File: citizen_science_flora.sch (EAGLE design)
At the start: 90 parts, among them IC1 W25Q64JVXGIQ, J1 SM03B-SRSS-TB(LF)(SN), J2 TYPE-C-31-M-12, J4 60312202114511, J5 60312202114511, U1 RP2350A, U2 APS6404L-3SQR-ZR, U3 ESP32-C3-MINI-1-N4, U4 MIC5504-3.3YM5-T5, U5 BME690, U6 ADM3260ARSZ, U7 ENS210-LQFM, U8 SFH6325-X017TEL0631, U9 AS3935-BQFT, Y1 12MHz

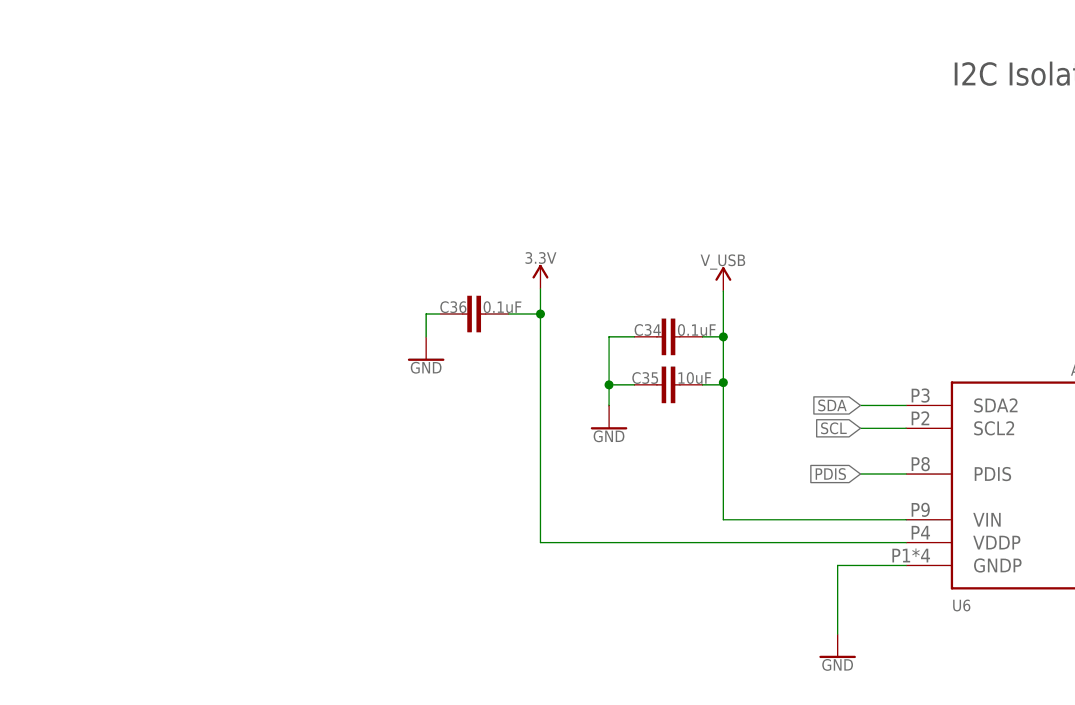
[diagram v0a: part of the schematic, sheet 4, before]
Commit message: placed some components
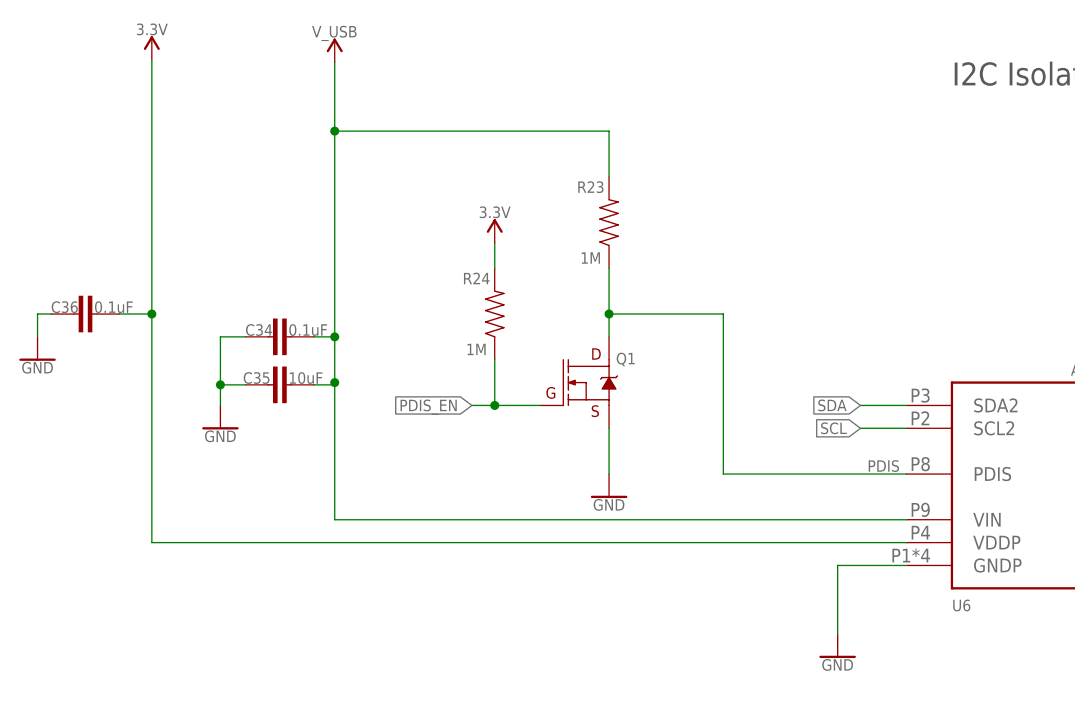
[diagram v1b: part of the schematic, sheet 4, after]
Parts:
- added Q1: 220mA/50V/3.5Ω, SparkFun-DiscreteSemi:MOSFET-NCH-BSS138
- added R23, R24: 1M, SparkFun-Resistors:1MOHM-0402-1/16W-5%
- J1: value SM03B-SRSS-TB(LF)(SN) -> BM03B-SRSS-TB(LF)(SN); device SM03B-SRSS-TB_LF__SN_:SM03B-SRSS-TB(LF)(SN) -> BM03B-SRSS-TB_LF__SN_:BM03B-SRSS-TB(LF)(SN)
- R12: value 10K -> 2.2K
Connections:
- new net PDIS_EN: Q1.G, R24.1, U1.GPIO8
- net 3.3V: now also R24.2
- net GND: now also Q1.S
- net PDIS: now also Q1.D, R23.1; no longer U1.GPIO8
- net V_USB: now also R23.2
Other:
- moved on the sheet: C34, C35, C36

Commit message: Add 3D packages to resistors
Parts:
- added C42: 0.1uF, SparkFun-Capacitors:0.1UF-0402T-16V-10%-X7R-WE
- USB: value TPB1,27 -> V_USB
- renumbered TP1 to USB, TP2 to GND, TP3 to 3.3V
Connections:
- net 3.3V: now also C42.2
- net GND: now also C42.1

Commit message: Board file updates
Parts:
- added C43: RSCSK2043R3D01004T, SamacSys_Parts:RSCSK2043R3D01004T
- added C44, C45, C46, C49, C50, C51, C52: 0.1uF, SparkFun-Capacitors:0.1UF-0402-6.3V-10%-X7R
- added C47, C48: 12pF, SparkFun-Capacitors:12PF-0402-50V-5%
- added D1: 1N4148, SparkFun-DiscreteSemi:DIODE-SCHOTTKY-BAT60A
- added D2: 1N5819, SparkFun-DiscreteSemi:DIODE-SCHOTTKY-BAT20J
- added J6: TSM-102-02-S-SH, TSM-102-02-S-SH:TSM-102-02-S-SH
- added LS1: MLT-8530, CMT-8504-100-SMT-TR:CMT-8504-100-SMT-TR
- added Q2: BSS138, SparkFun-DiscreteSemi:MOSFET-NCH-2N7002PW
- added R25: 470, SparkFun-Resistors:10KOHM-0402-1/16W-1%
- added U10: PCF8563T/F4,118, PCF8563T_F4_118:PCF8563T/F4,118
- added U11, U12, U13, U14: OPS-S56AAF5, OPS=S56AAF5:OPS-S56AAF5
- added U15: SN74LVC1T45DBVRG4, SN74LVC1T45DBVRG4:SN74LVC1T45DBVRG4
- added USR_BUTTON: MOMENTARY-SWITCH-SPST-SMD-4.6X2.8MM, SparkFun-Switches:MOMENTARY-SWITCH-SPST-SMD-4.6X2.8MM
- added XTAL1: Q13FC1350000400, Q13FC1350000400:Q13FC1350000400
- J1: value BM03B-SRSS-TB(LF)(SN) -> SM03B-SRSS-TB(LF)(SN); device BM03B-SRSS-TB_LF__SN_:BM03B-SRSS-TB(LF)(SN) -> SM03B-SRSS-TB_LF__SN_:SM03B-SRSS-TB(LF)(SN)
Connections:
- new net BUZZER_DRIVER: R25.2, U1.GPIO6
- new net INT_RTC: U1.GPIO26/ADC0, U10.~INT
- new net N$22: U11.DO, U12.DI
- new net N$23: U12.DO, U13.DI
- new net N$24: U13.DO, U14.DI
- new net N$25: U1.GPIO3, USR_BUTTON.1
- new net N$26: D1.A, LS1.N, Q2.D
- new net N$27: Q2.G, R25.1
- new net N$28: C43.+, C46.1, D2.C, U10.VDD
- new net N$29: C48.2, U10.OSCO, XTAL1.1
- new net N$30: C47.2, U10.OSCI, XTAL1.2
- new net NEOPIXEL_3.3V: U1.GPIO16, U15.A
- new net NEOPIXEL_5V: U11.DI, U15.B
- net 3.3V: now also C44.2, D1.C, D2.A, LS1.P, U15.DIR, U15.VCCA
- net GND: now also C43.-, C44.1, C45.2, C46.2, C47.1, C48.1, C49.2, C50.2, C51.2, C52.2, Q2.S, U10.VSS, U11.GND, U12.GND, U13.GND, U14.GND, U15.GND, USR_BUTTON.2
- net SCL: now also U10.SCL
- net SDA: now also U10.SDA
- net V_USB: now also C45.1, C49.1, C50.1, C51.1, C52.1, U11.VCC, U12.VCC, U13.VCC, U14.VCC, U15.VCCB
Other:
- note added: "Buzzer Driver"
- note added: "Level Shifter"
- note added: "Neopixel Seven Segment"
- note added: "RTC"
- moved on the sheet: C20, C21, C22, C23, C24, C26, C27, C29, C30, C31, C32, C33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

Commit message: Updates to the design
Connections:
- net N$18 renamed PRB1
- net N$19 renamed PRB1_GND
- net N$20 renamed PROBE2_GND
- net N$21 renamed PROBE2
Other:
- moved on the sheet: J5
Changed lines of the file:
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@@
 <attribute name="VALUE" x="38.1" y="47.752" size="1.27" layer="96" font="vector" ratio="20" align="bottom-center"/>
 </instance>
-<instance part="J5" gate="G$1" x="172.72" y="53.34" smashed="yes">
-<attribute name="NAME" x="168.91" y="54.356" size="1.27" layer="95" font="vector" ratio="20" align="bottom-center"/>
-<attribute name="VALUE" x="172.72" y="45.212" size="1.27" layer="96" font="vector" ratio="20" align="bottom-center"/>
+<instance part="J5" gate="G$1" x="166.878" y="53.34" smashed="yes">
+<attribute name="NAME" x="163.068" y="54.356" size="1.27" layer="95" font="vector" ratio="20" align="bottom-center"/>
+<attribute name="VALUE" x="166.878" y="45.212" size="1.27" layer="96" font="vector" ratio="20" align="bottom-center"/>
 </instance>
 <instance part="U$6" gate="G$1" x="170.18" y="78.74" smashed="yes">
@@
 </segment>
 </net>
-<net name="N$18" class="0">
-<segment>
-<pinref part="J4" gate="G$1" pin="1"/>
-<pinref part="U$2" gate="G$1" pin="PRB"/>
-<wire x1="45.72" y1="55.88" x2="58.42" y2="55.88" width="0.1524" layer="91"/>
-</segment>
-</net>
-<net name="N$19" class="0">
-<segment>
-<pinref part="J4" gate="G$1" pin="2"/>
-<pinref part="U$2" gate="G$1" pin="PRB_GND"/>
-<wire x1="45.72" y1="50.8" x2="58.42" y2="50.8" width="0.1524" layer="91"/>
-</segment>
-</net>
-<net name="N$20" class="0">
-<segment>
-<pinref part="J5" gate="G$1" pin="2"/>
-<pinref part="U$3" gate="G$1" pin="PRB_GND"/>
-<wire x1="180.34" y1="48.26" x2="185.42" y2="48.26" width="0.1524" layer="91"/>
-</segment>
-</net>
-<net name="N$21" class="0">
-<segment>
-<pinref part="J5" gate="G$1" pin="1"/>
-<pinref part="U$3" gate="G$1" pin="PRB"/>
-<wire x1="180.34" y1="53.34" x2="185.42" y2="53.34" width="0.1524" layer="91"/>
-</segment>
-</net>
 <net name="PDIS_EN" class="0">
 <segment>
@@
 </segment>
 </net>
+<net name="PRB1" class="0">
+<segment>
+<pinref part="J4" gate="G$1" pin="1"/>
+<pinref part="U$2" gate="G$1" pin="PRB"/>
+<wire x1="45.72" y1="55.88" x2="58.42" y2="55.88" width="0.1524" layer="91"/>
+<label x="48.26" y="55.88" size="1.27" layer="95" font="vector" ratio="20"/>
+</segment>
+</net>
+<net name="PRB1_GND" class="0">
+<segment>
+<pinref part="J4" gate="G$1" pin="2"/>
+<pinref part="U$2" gate="G$1" pin="PRB_GND"/>
+<wire x1="45.72" y1="50.8" x2="58.42" y2="50.8" width="0.1524" layer="91"/>
+<label x="48.26" y="50.8" size="1.27" layer="95" font="vector" ratio="20"/>
+</segment>
+</net>
+<net name="PROBE2" class="0">
+<segment>
+<pinref part="J5" gate="G$1" pin="1"/>
+<pinref part="U$3" gate="G$1" pin="PRB"/>
+<wire x1="174.498" y1="53.34" x2="185.42" y2="53.34" width="0.1524" layer="91"/>
+<label x="177.8" y="53.34" size="1.27" layer="95" font="vector" ratio="20"/>
+</segment>
+</net>
+<net name="PROBE2_GND" class="0">
+<segment>
+<pinref part="J5" gate="G$1" pin="2"/>
+<pinref part="U$3" gate="G$1" pin="PRB_GND"/>
+<wire x1="174.498" y1="48.26" x2="185.42" y2="48.26" width="0.1524" layer="91"/>
+<label x="175.514" y="48.26" size="1.27" layer="95" font="vector" ratio="20"/>
+</segment>
+</net>
